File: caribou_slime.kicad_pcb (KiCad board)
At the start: 2 copper layers, 62.7 x 37.6 mm, 37 parts, among them J1 BATT JST, Q1 AO3145, U1 ESP32-C3_SUPERMINI, U2 BMI270, U3 FS312F-G, U4 FS8205A, U5 TP4056, U6 ME6211C33M5G

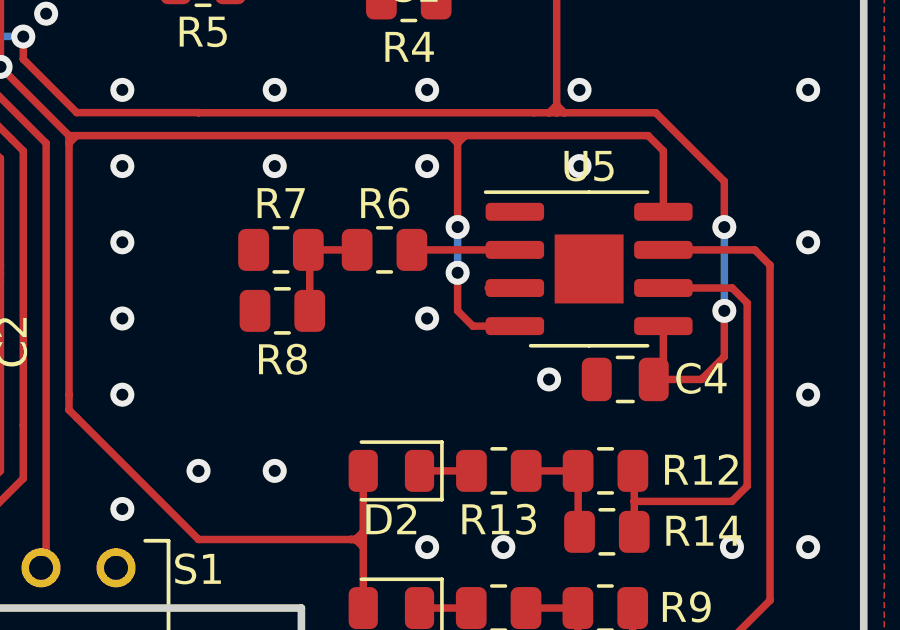
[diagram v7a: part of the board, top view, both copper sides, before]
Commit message: fix(pcb): Rework TP4056 pin 3 to properly ground
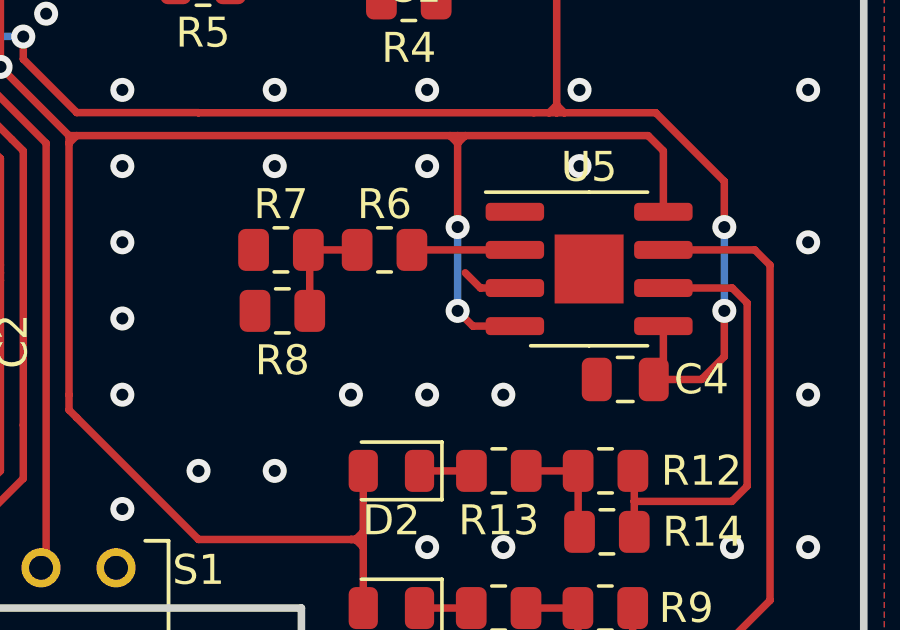
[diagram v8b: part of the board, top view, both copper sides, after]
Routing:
- net GND: track 5.78 -> 6.75 mm, vias 54 -> 55
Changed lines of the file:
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@@
   (segment (start 53.274 25.72) (end 53.34 25.654) (width 0.25) (layer "F.Cu") (net 9))
   (segment (start 59.436 37.338) (end 59.440653 37.333347) (width 0.25) (layer "F.Cu") (net 9))
-  (segment (start 74.676 44.196) (end 74.676 45.466) (width 0.25) (layer "F.Cu") (net 9))
   (segment (start 55.118 25.654) (end 55.372 25.654) (width 0.25) (layer "F.Cu") (net 9))
   (segment (start 74.676 39.878) (end 74.676 42.672) (width 0.25) (layer "F.Cu") (net 9))
@@
   (via (at 49.784 38.608) (size 0.8) (drill 0.4) (layers "F.Cu" "B.Cu") (net 9))
   (via (at 37.084 38.608) (size 0.8) (drill 0.4) (layers "F.Cu" "B.Cu") (net 9))
-  (via (at 74.676 44.196) (size 0.8) (drill 0.4) (layers "F.Cu" "B.Cu") (net 9))
   (via (at 74.676 42.672) (size 0.8) (drill 0.4) (layers "F.Cu" "B.Cu") (net 9))
+  (via (at 74.676 45.466) (size 0.8) (drill 0.4) (layers "F.Cu" "B.Cu") (net 9))
   (via (at 26.924 39.116) (size 0.8) (drill 0.4) (layers "F.Cu" "B.Cu") (net 9))
   (via (at 59.440653 37.333347) (size 0.8) (drill 0.4) (layers "F.Cu" "B.Cu") (net 9))
   (segment (start 58.166 38.608) (end 59.440653 37.333347) (width 0.25) (layer "B.Cu") (net 9))
+  (segment (start 74.676 42.672) (end 74.676 45.466) (width 0.25) (layer "B.Cu") (net 9))
   (segment (start 49.784 38.608) (end 58.166 38.608) (width 0.25) (layer "B.Cu") (net 9))
   (segment (start 26.924 39.116) (end 27.432 38.608) (width 0.25) (layer "B.Cu") (net 9))
   (segment (start 27.432 38.608) (end 37.084 38.608) (width 0.25) (layer "B.Cu") (net 9))
-  (segment (start 74.676 42.672) (end 74.676 44.196) (width 0.25) (layer "B.Cu") (net 9))
+  (segment (start 75.438 44.704) (end 74.93 44.196) (width 0.25) (layer "F.Cu") (net 13))
   (segment (start 53.0555 45.478) (end 52.082 45.478) (width 0.25) (layer "F.Cu") (net 13))
+  (segment (start 76.584 44.704) (end 75.438 44.704) (width 0.25) (layer "F.Cu") (net 13))
   (segment (start 52.082 45.478) (end 52.07 45.466) (width 0.25) (layer "F.Cu") (net 13))
   (segment (start 66.619 32.5805) (end 66.619 33.4954) (width 0.25) (layer "F.Cu") (net 13))
@@
   (segment (start 54.407 47.3275) (end 54.407 48.463) (width 0.25) (layer "F.Cu") (net 13))
   (segment (start 66.619 33.4954) (end 65.5704 34.544) (width 0.25) (layer "F.Cu") (net 13))
-  (segment (start 76.584 44.704) (end 75.692 44.704) (width 0.25) (layer "F.Cu") (net 13))
   (segment (start 54.407 48.463) (end 54.356 48.514) (width 0.25) (layer "F.Cu") (net 13))
   (via (at 50.8 43.18) (size 0.8) (drill 0.4) (layers "F.Cu" "B.Cu") (free) (net 13))
@@
   (via (at 66.04 50.8) (size 0.8) (drill 0.4) (layers "F.Cu" "B.Cu") (free) (net 13))
   (via (at 38.1 39.624) (size 0.8) (drill 0.4) (layers "F.Cu" "B.Cu") (free) (net 13))
+  (via (at 71.12 48.26) (size 0.8) (drill 0.4) (layers "F.Cu" "B.Cu") (free) (net 13))
   (via (at 50.8 50.8) (size 0.8) (drill 0.4) (layers "F.Cu" "B.Cu") (free) (net 13))
   (via (at 43.18 48.26) (size 0.8) (drill 0.4) (layers "F.Cu" "B.Cu") (free) (net 13))
   (via (at 73.66 38.1) (size 0.8) (drill 0.4) (layers "F.Cu" "B.Cu") (free) (net 13))
-  (via (at 77.724 47.752) (size 0.8) (drill 0.4) (layers "F.Cu" "B.Cu") (free) (net 13))
+  (via (at 76.2 48.26) (size 0.8) (drill 0.4) (layers "F.Cu" "B.Cu") (free) (net 13))
   (via (at 78.74 38.1) (size 0.8) (drill 0.4) (layers "F.Cu" "B.Cu") (free) (net 13))
   (via (at 83.82 53.34) (size 0.8) (drill 0.4) (layers "F.Cu" "B.Cu") (free) (net 13))
@@
   (via (at 55.88 48.26) (size 0.8) (drill 0.4) (layers "F.Cu" "B.Cu") (free) (net 13))
   (via (at 76.2 53.34) (size 0.8) (drill 0.4) (layers "F.Cu" "B.Cu") (free) (net 13))
-  (via (at 73.66 45.72) (size 0.8) (drill 0.4) (layers "F.Cu" "B.Cu") (free) (net 13))
   (via (at 63.5 43.18) (size 0.8) (drill 0.4) (layers "F.Cu" "B.Cu") (free) (net 13))
   (via (at 60.96 30.48) (size 0.8) (drill 0.4) (layers "F.Cu" "B.Cu") (free) (net 13))
@@
   (via (at 50.8 48.26) (size 0.8) (drill 0.4) (layers "F.Cu" "B.Cu") (free) (net 13))
   (via (at 86.36 38.1) (size 0.8) (drill 0.4) (layers "F.Cu" "B.Cu") (free) (net 13))
+  (via (at 73.66 48.26) (size 0.8) (drill 0.4) (layers "F.Cu" "B.Cu") (free) (net 13))
   (via (at 86.36 43.18) (size 0.8) (drill 0.4) (layers "F.Cu" "B.Cu") (free) (net 13))
   (via (at 58.42 40.64) (size 0.8) (drill 0.4) (layers "F.Cu" "B.Cu") (free) (net 13))
